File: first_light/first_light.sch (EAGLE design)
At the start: 56 parts, among them IC1 MC34063AD, J1 DCJ0202, J2 DCJ0202, Q1 ZXMN4A06GTA, U1 STM32F051C6T6, X1 8MHz, Y1 32.768kHz

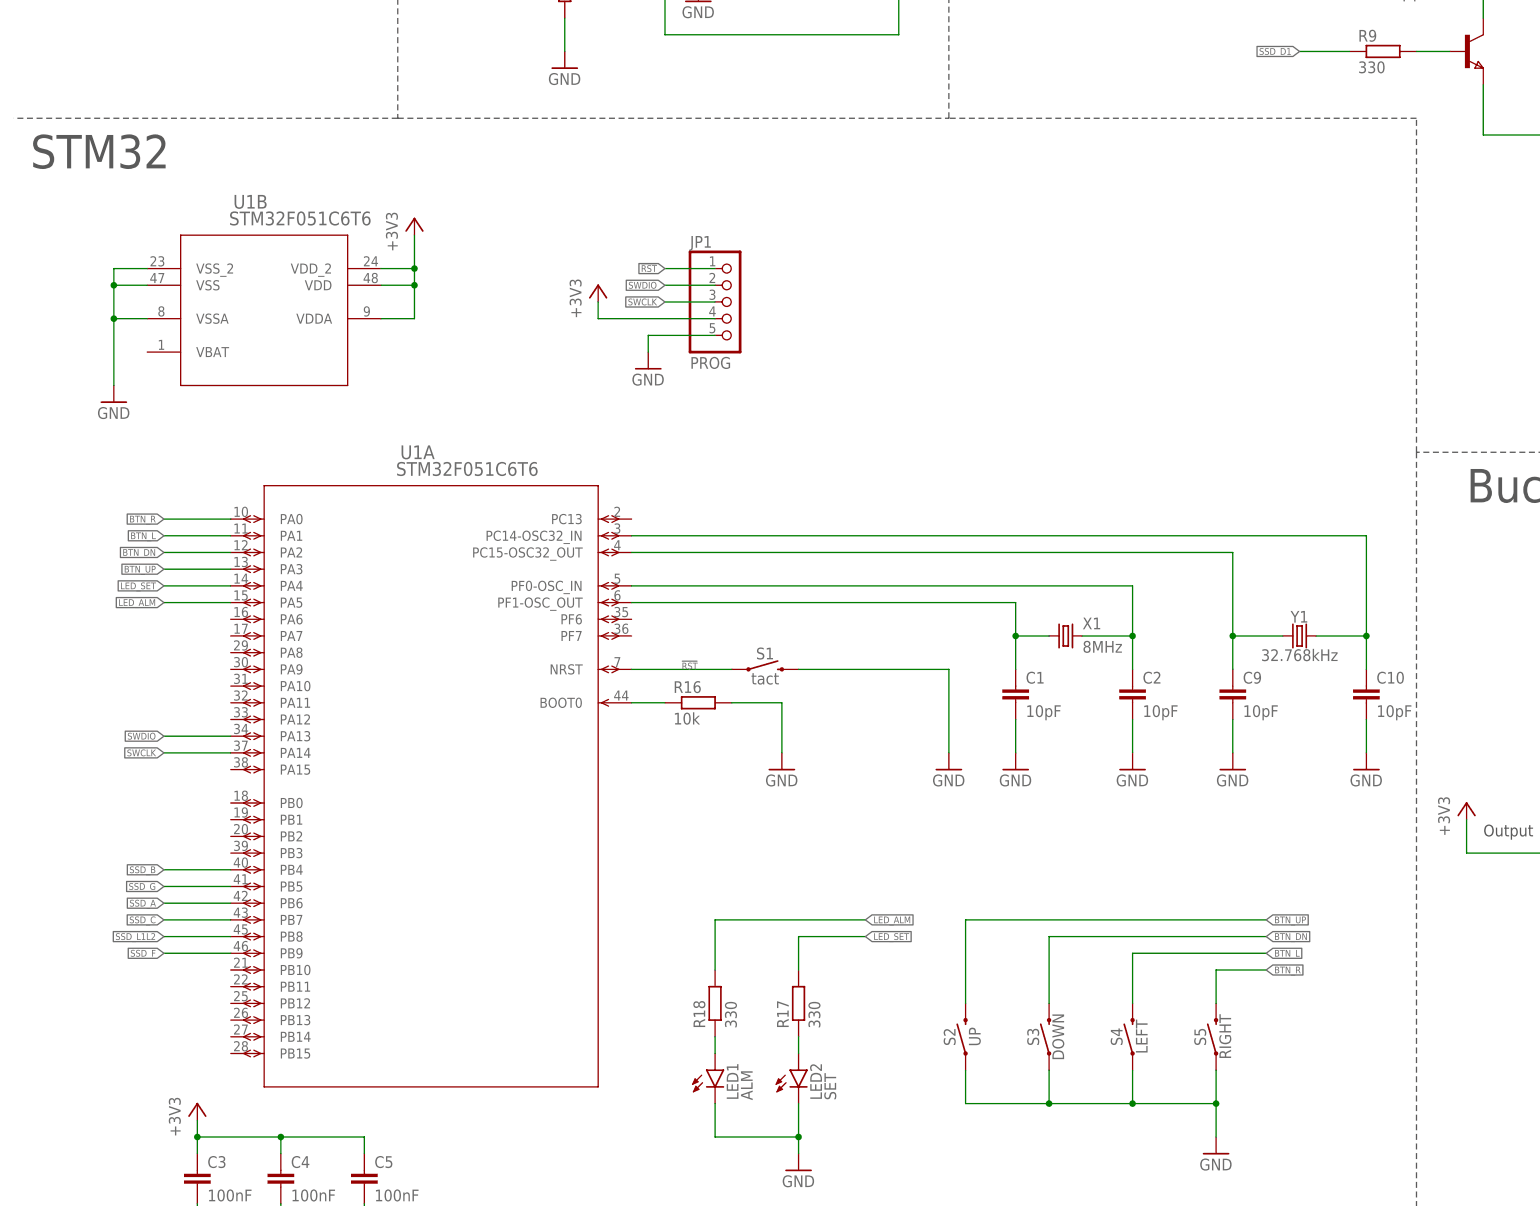
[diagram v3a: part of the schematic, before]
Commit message: now using esp32 due to no stm available
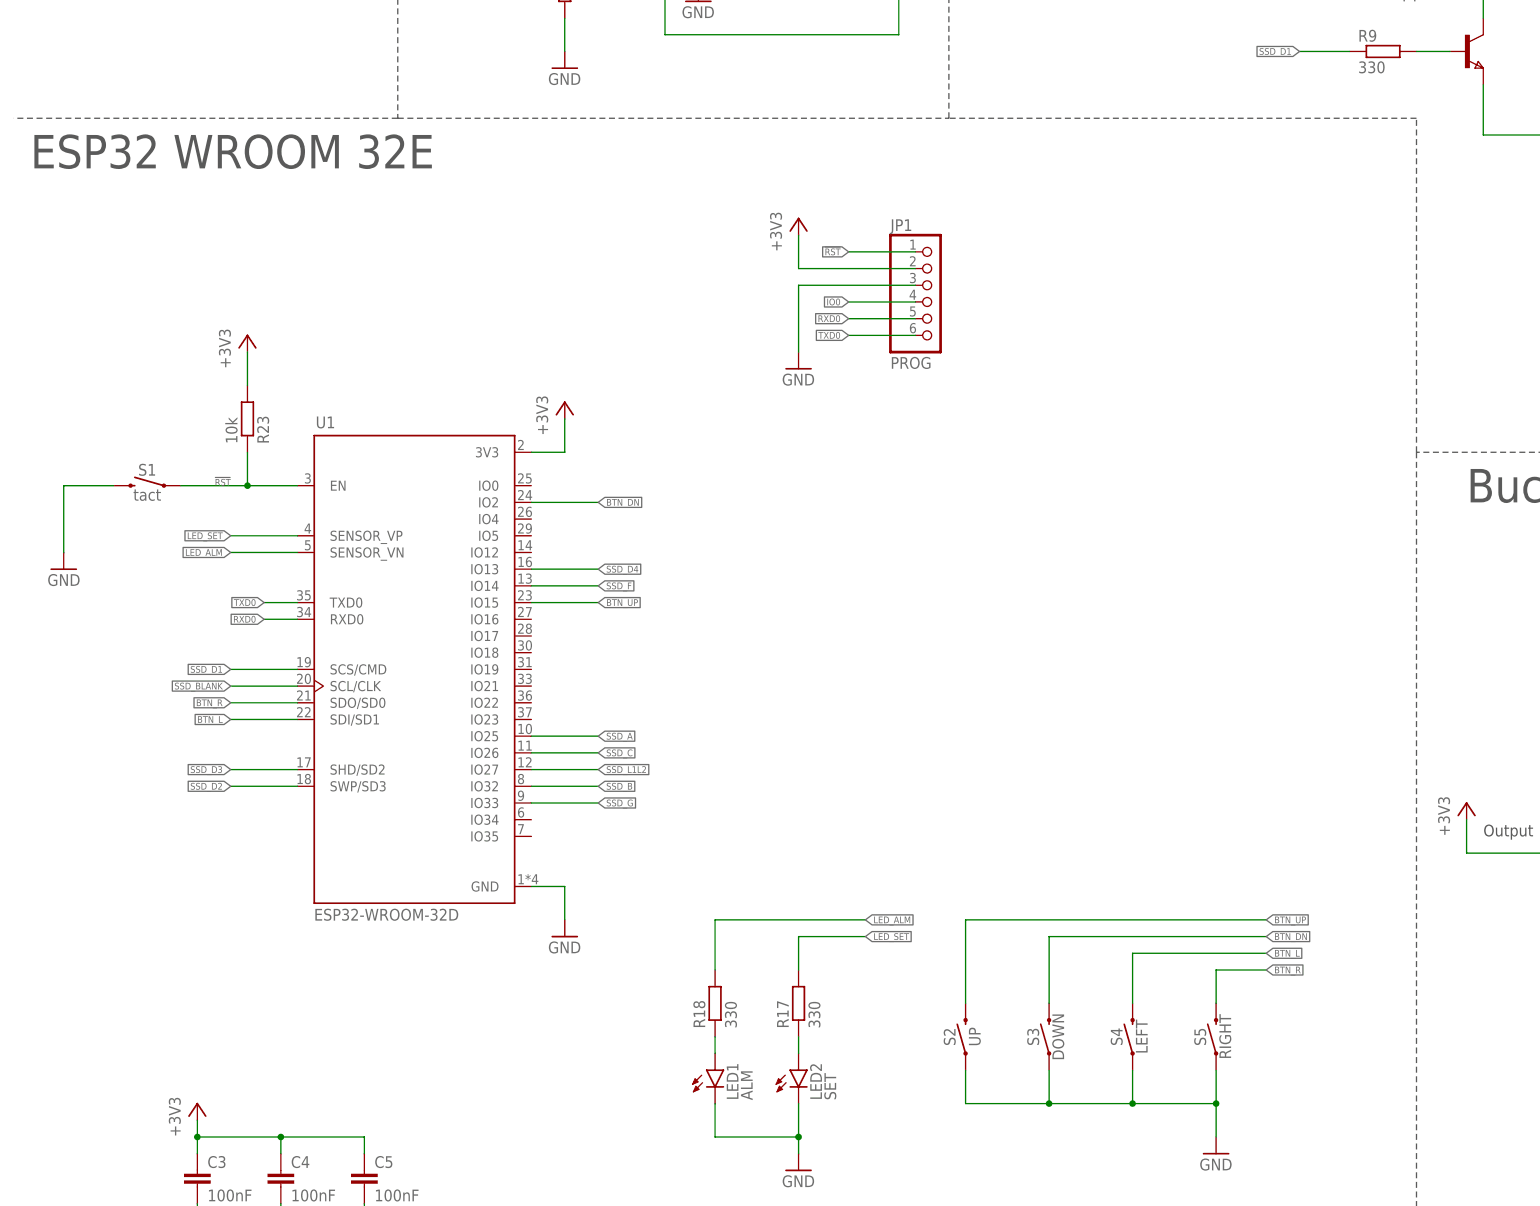
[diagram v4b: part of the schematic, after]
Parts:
- removed C1, C10, C2, C9: 10pF, rcl:C-EUC0603
- removed R16: 10k, rcl:R-EU_R0603
- removed X1: 8MHz, IQD-Frequency-Products:CRYSTALS-NOGND-4-HSMX
- removed Y1: 32.768kHz, SparkFun-Clocks:CRYSTAL-32.768KHZSMD-3.2X1.5
- added R23: 10k, rcl:R-EU_R0603
- JP1: device pinhead:PINHD-1X5 -> pinhead:PINHD-1X6
- U1: value STM32F051C6T6 -> ESP32-WROOM-32D; device STM32F051C6:STM32F051C6T6 -> ESP32-WROOM-32D:ESP32-WROOM-32D
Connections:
- removed net N$14: C1.1, U1A.PF1-OSC_OUT, X1.1
- removed net N$20: C2.1, U1A.PF0-OSC_IN, X1.2
- removed net N$25: R16.1, U1A.BOOT0
- removed net N$30: C9.1, U1A.PC15-OSC32_OUT, Y1.1
- removed net N$31: C10.1, U1A.PC14-OSC32_IN, Y1.2
- removed net SWCLK: JP1.3, U1A.PA14
- removed net SWDIO: JP1.2, U1A.PA13
- new net IO0: JP1.4
- new net RXD0: JP1.5, U1.RXD0
- new net TXD0: JP1.6, U1.TXD0
- net !RST: now also R23.1, U1.EN; no longer U1A.NRST
- net +3V3: now also JP1.2, R23.2, U1.3V3; no longer JP1.4, U1B.VDD, U1B.VDDA, U1B.VDD_2
- net BTN_DN: now also U1.IO2; no longer U1A.PA2
- net BTN_L: now also U1.SDI/SD1; no longer U1A.PA1
- net BTN_R: now also U1.SDO/SD0; no longer U1A.PA0
- net BTN_UP: now also U1.IO15; no longer U1A.PA3
- net GND: now also JP1.3, U1.GND; no longer C1.2, C10.2, C2.2, C9.2, JP1.5, R16.2, U1B.VSS, U1B.VSSA, U1B.VSS_2
- net LED_ALM: now also U1.SENSOR_VN; no longer U1A.PA5
- net LED_SET: now also U1.SENSOR_VP; no longer U1A.PA4
- net SSD_A: now also U1.IO25; no longer U1A.PB6
- net SSD_B: now also U1.IO32; no longer U1A.PB4
- net SSD_BLANK: now also U1.SCL/CLK
- net SSD_C: now also U1.IO26; no longer U1A.PB7
- net SSD_D1: now also U1.SCS/CMD
- net SSD_D2: now also U1.SWP/SD3
- net SSD_D3: now also U1.SHD/SD2
- net SSD_D4: now also U1.IO13
- net SSD_F: now also U1.IO14; no longer U1A.PB9
- net SSD_G: now also U1.IO33; no longer U1A.PB5
- net SSD_L1L2: now also U1.IO27; no longer U1A.PB8
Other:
- note added: "ESP32 WROOM 32E"
- note removed: "STM32"
- moved on the sheet: S1

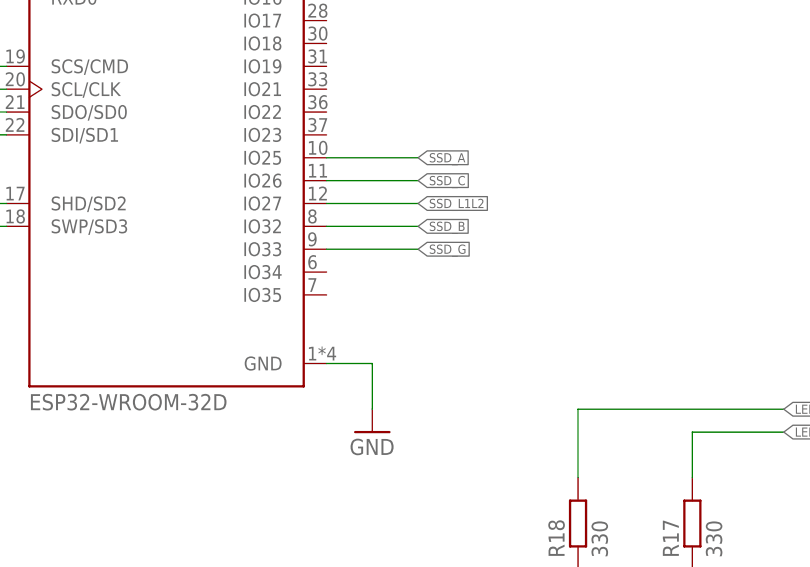
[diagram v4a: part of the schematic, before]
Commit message: wired up ssd to esp
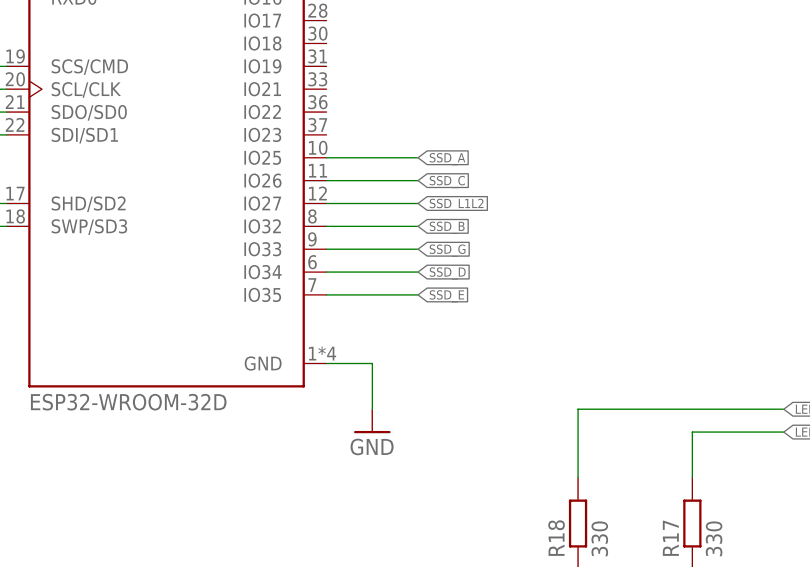
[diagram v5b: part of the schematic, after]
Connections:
- net SSD_D: now also U1.IO34
- net SSD_E: now also U1.IO35
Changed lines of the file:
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@@
 <label x="243.84" y="218.44" size="1.016" layer="95" xref="yes"/>
+</segment>
+<segment>
+<pinref part="U1" gate="G$1" pin="IO34"/>
+<wire x1="83.82" y1="76.2" x2="93.98" y2="76.2" width="0.1524" layer="91"/>
+<label x="93.98" y="76.2" size="1.016" layer="95" xref="yes"/>
 </segment>
 </net>
@@
 <label x="243.84" y="228.6" size="1.016" layer="95" xref="yes"/>
 </segment>
+<segment>
+<pinref part="U1" gate="G$1" pin="IO35"/>
+<wire x1="83.82" y1="73.66" x2="93.98" y2="73.66" width="0.1524" layer="91"/>
+<label x="93.98" y="73.66" size="1.016" layer="95" xref="yes"/>
+</segment>
 </net>

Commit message: finished layout and routing
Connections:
- net BTN_DN: now also U1.SDI/SD1; no longer U1.IO2
- net BTN_L: now also U1.IO15; no longer U1.SDI/SD1
- net BTN_R: now also U1.IO2; no longer U1.SDO/SD0
- net BTN_UP: now also U1.SDO/SD0; no longer U1.IO15
- net IO0: now also U1.IO0
- net LED_PWM: now also U1.IO12
- net SSD_A: now also U1.IO33; no longer U1.IO25
- net SSD_B: now also U1.IO26; no longer U1.IO32
- net SSD_C: now also U1.IO32; no longer U1.IO26
- net SSD_D: now also U1.IO27; no longer U1.IO34
- net SSD_E: now also U1.IO14; no longer U1.IO35
- net SSD_F: now also U1.IO34; no longer U1.IO14
- net SSD_G: now also U1.IO25; no longer U1.IO33
- net SSD_L1L2: now also U1.IO35; no longer U1.IO27
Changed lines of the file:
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@@
+</segment>
+<segment>
+<wire x1="83.82" y1="83.82" x2="93.98" y2="83.82" width="0.1524" layer="91"/>
+<label x="93.98" y="83.82" size="1.016" layer="95" xref="yes"/>
+<pinref part="U1" gate="G$1" pin="IO27"/>
+</segment>
+</net>
+<net name="SSD_E" class="0">
+<segment>
+<pinref part="R8" gate="G$1" pin="2"/>
+<wire x1="238.76" y1="228.6" x2="243.84" y2="228.6" width="0.1524" layer="91"/>
+<label x="243.84" y="228.6" size="1.016" layer="95" xref="yes"/>
+</segment>
+<segment>
+<wire x1="83.82" y1="111.76" x2="93.98" y2="111.76" width="0.1524" layer="91"/>
+<label x="93.98" y="111.76" size="1.016" layer="95" xref="yes"/>
+<pinref part="U1" gate="G$1" pin="IO14"/>
+</segment>
+</net>
+<net name="SSD_F" class="0">
+<segment>
+<pinref part="R1" gate="G$1" pin="1"/>
+<wire x1="170.18" y1="233.68" x2="165.1" y2="233.68" width="0.1524" layer="91"/>
+<label x="165.1" y="233.68" size="1.016" layer="95" rot="R180" xref="yes"/>
 </segment>
 <segment>
@@
 </segment>
 </net>
-<net name="SSD_E" class="0">
-<segment>
-<pinref part="R8" gate="G$1" pin="2"/>
-<wire x1="238.76" y1="228.6" x2="243.84" y2="228.6" width="0.1524" layer="91"/>
-<label x="243.84" y="228.6" size="1.016" layer="95" xref="yes"/>
+<net name="SSD_L1L2" class="0">
+<segment>
+<pinref part="R2" gate="G$1" pin="1"/>
+<wire x1="170.18" y1="228.6" x2="165.1" y2="228.6" width="0.1524" layer="91"/>
+<label x="165.1" y="228.6" size="1.016" layer="95" rot="R180" xref="yes"/>
 </segment>
 <segment>
@@
 </segment>
 </net>
-<net name="SSD_F" class="0">
-<segment>
-<pinref part="R1" gate="G$1" pin="1"/>
-<wire x1="170.18" y1="233.68" x2="165.1" y2="233.68" width="0.1524" layer="91"/>
-<label x="165.1" y="233.68" size="1.016" layer="95" rot="R180" xref="yes"/>
-</segment>
-<segment>
-<wire x1="83.82" y1="111.76" x2="93.98" y2="111.76" width="0.1524" layer="91"/>
-<label x="93.98" y="111.76" size="1.016" layer="95" xref="yes"/>
-<pinref part="U1" gate="G$1" pin="IO14"/>
-</segment>
-</net>
-<net name="SSD_L1L2" class="0">
-<segment>
-<pinref part="R2" gate="G$1" pin="1"/>
-<wire x1="170.18" y1="228.6" x2="165.1" y2="228.6" width="0.1524" layer="91"/>
-<label x="165.1" y="228.6" size="1.016" layer="95" rot="R180" xref="yes"/>
-</segment>
-<segment>
-<wire x1="83.82" y1="83.82" x2="93.98" y2="83.82" width="0.1524" layer="91"/>
-<label x="93.98" y="83.82" size="1.016" layer="95" xref="yes"/>
-<pinref part="U1" gate="G$1" pin="IO27"/>
-</segment>
-</net>
 <net name="SSD_C" class="0">
 <segment>
@@
 </segment>
 <segment>
+<wire x1="83.82" y1="81.28" x2="93.98" y2="81.28" width="0.1524" layer="91"/>
+<label x="93.98" y="81.28" size="1.016" layer="95" xref="yes"/>
+<pinref part="U1" gate="G$1" pin="IO32"/>
+</segment>
+</net>
+<net name="SSD_A" class="0">
+<segment>
+<pinref part="R4" gate="G$1" pin="1"/>
+<wire x1="170.18" y1="218.44" x2="165.1" y2="218.44" width="0.1524" layer="91"/>
+<label x="165.1" y="218.44" size="1.016" layer="95" rot="R180" xref="yes"/>
+</segment>
+<segment>
+<wire x1="83.82" y1="78.74" x2="93.98" y2="78.74" width="0.1524" layer="91"/>
+<label x="93.98" y="78.74" size="1.016" layer="95" xref="yes"/>
+<pinref part="U1" gate="G$1" pin="IO33"/>
+</segment>
+</net>
+<net name="SSD_G" class="0">
+<segment>
+<pinref part="R5" gate="G$1" pin="1"/>
+<wire x1="170.18" y1="213.36" x2="165.1" y2="213.36" width="0.1524" layer="91"/>
+<label x="165.1" y="213.36" size="1.016" layer="95" rot="R180" xref="yes"/>
+</segment>
+<segment>
+<wire x1="83.82" y1="88.9" x2="93.98" y2="88.9" width="0.1524" layer="91"/>
+<label x="93.98" y="88.9" size="1.016" layer="95" xref="yes"/>
+<pinref part="U1" gate="G$1" pin="IO25"/>
+</segment>
+</net>
+<net name="SSD_B" class="0">
+<segment>
+<pinref part="R6" gate="G$1" pin="1"/>
+<wire x1="170.18" y1="208.28" x2="165.1" y2="208.28" width="0.1524" layer="91"/>
+<label x="165.1" y="208.28" size="1.016" layer="95" rot="R180" xref="yes"/>
+</segment>
+<segment>
 <wire x1="83.82" y1="86.36" x2="93.98" y2="86.36" width="0.1524" layer="91"/>
 <label x="93.98" y="86.36" size="1.016" layer="95" xref="yes"/>
 <pinref part="U1" gate="G$1" pin="IO26"/>
-</segment>
-</net>
-<net name="SSD_A" class="0">
-<segment>
-<pinref part="R4" gate="G$1" pin="1"/>
-<wire x1="170.18" y1="218.44" x2="165.1" y2="218.44" width="0.1524" layer="91"/>
-<label x="165.1" y="218.44" size="1.016" layer="95" rot="R180" xref="yes"/>
-</segment>
-<segment>
-<wire x1="83.82" y1="88.9" x2="93.98" y2="88.9" width="0.1524" layer="91"/>
-<label x="93.98" y="88.9" size="1.016" layer="95" xref="yes"/>
-<pinref part="U1" gate="G$1" pin="IO25"/>
-</segment>
-</net>
-<net name="SSD_G" class="0">
-<segment>
-<pinref part="R5" gate="G$1" pin="1"/>
-<wire x1="170.18" y1="213.36" x2="165.1" y2="213.36" width="0.1524" layer="91"/>
-<label x="165.1" y="213.36" size="1.016" layer="95" rot="R180" xref="yes"/>
-</segment>
-<segment>
-<wire x1="83.82" y1="78.74" x2="93.98" y2="78.74" width="0.1524" layer="91"/>
-<label x="93.98" y="78.74" size="1.016" layer="95" xref="yes"/>
-<pinref part="U1" gate="G$1" pin="IO33"/>
-</segment>
-</net>
-<net name="SSD_B" class="0">
-<segment>
-<pinref part="R6" gate="G$1" pin="1"/>
-<wire x1="170.18" y1="208.28" x2="165.1" y2="208.28" width="0.1524" layer="91"/>
-<label x="165.1" y="208.28" size="1.016" layer="95" rot="R180" xref="yes"/>
-</segment>
-<segment>
-<wire x1="83.82" y1="81.28" x2="93.98" y2="81.28" width="0.1524" layer="91"/>
-<label x="93.98" y="81.28" size="1.016" layer="95" xref="yes"/>
-<pinref part="U1" gate="G$1" pin="IO32"/>
 </segment>
 </net>
@@
 <label x="83.82" y="213.36" size="1.016" layer="95" rot="R180" xref="yes"/>
 </segment>
+<segment>
+<pinref part="U1" gate="G$1" pin="IO12"/>
+<wire x1="83.82" y1="116.84" x2="93.98" y2="116.84" width="0.1524" layer="91"/>
+<label x="93.98" y="116.84" size="1.016" layer="95" xref="yes"/>
+</segment>
 </net>
 <net name="N$23" class="0">
@@
 </segment>
 <segment>
-<wire x1="83.82" y1="109.22" x2="93.98" y2="109.22" width="0.1524" layer="91"/>
-<label x="93.98" y="109.22" size="1.016" layer="95" xref="yes"/>
-<pinref part="U1" gate="G$1" pin="IO15"/>
+<wire x1="48.26" y1="93.98" x2="38.1" y2="93.98" width="0.1524" layer="91"/>
+<label x="38.1" y="93.98" size="1.016" layer="95" rot="R180" xref="yes"/>
+<pinref part="U1" gate="G$1" pin="SDO/SD0"/>
 </segment>
 </net>
@@
 </segment>
 <segment>
-<wire x1="83.82" y1="124.46" x2="93.98" y2="124.46" width="0.1524" layer="91"/>
-<label x="93.98" y="124.46" size="1.016" layer="95" xref="yes"/>
-<pinref part="U1" gate="G$1" pin="IO2"/>
+<wire x1="48.26" y1="91.44" x2="38.1" y2="91.44" width="0.1524" layer="91"/>
+<label x="38.1" y="91.44" size="1.016" layer="95" rot="R180" xref="yes"/>
+<pinref part="U1" gate="G$1" pin="SDI/SD1"/>
 </segment>
 </net>
@@
 </segment>
 <segment>
-<wire x1="48.26" y1="91.44" x2="38.1" y2="91.44" width="0.1524" layer="91"/>
-<label x="38.1" y="91.44" size="1.016" layer="95" rot="R180" xref="yes"/>
-<pinref part="U1" gate="G$1" pin="SDI/SD1"/>
+<wire x1="83.82" y1="109.22" x2="93.98" y2="109.22" width="0.1524" layer="91"/>
+<label x="93.98" y="109.22" size="1.016" layer="95" xref="yes"/>
+<pinref part="U1" gate="G$1" pin="IO15"/>
 </segment>
 </net>
@@
 </segment>
 <segment>
-<wire x1="48.26" y1="93.98" x2="38.1" y2="93.98" width="0.1524" layer="91"/>
-<label x="38.1" y="93.98" size="1.016" layer="95" rot="R180" xref="yes"/>
-<pinref part="U1" gate="G$1" pin="SDO/SD0"/>
+<wire x1="83.82" y1="124.46" x2="93.98" y2="124.46" width="0.1524" layer="91"/>
+<label x="93.98" y="124.46" size="1.016" layer="95" xref="yes"/>
+<pinref part="U1" gate="G$1" pin="IO2"/>
 </segment>
 </net>
@@
 <label x="132.08" y="154.94" size="1.016" layer="95" rot="R180" xref="yes"/>
 </segment>
-</net>
+<segment>
+<pinref part="U1" gate="G$1" pin="IO0"/>
+<wire x1="83.82" y1="127" x2="93.98" y2="127" width="0.1524" layer="91"/>
+<label x="93.98" y="127" size="1.016" layer="95" xref="yes"/>
+</segment>
+</net>
